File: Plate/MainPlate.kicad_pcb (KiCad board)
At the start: 2 copper layers, 139.1 x 77.2 mm, 4 parts, among them J1 Conn_01x03, SW1 Test, SW2 Service

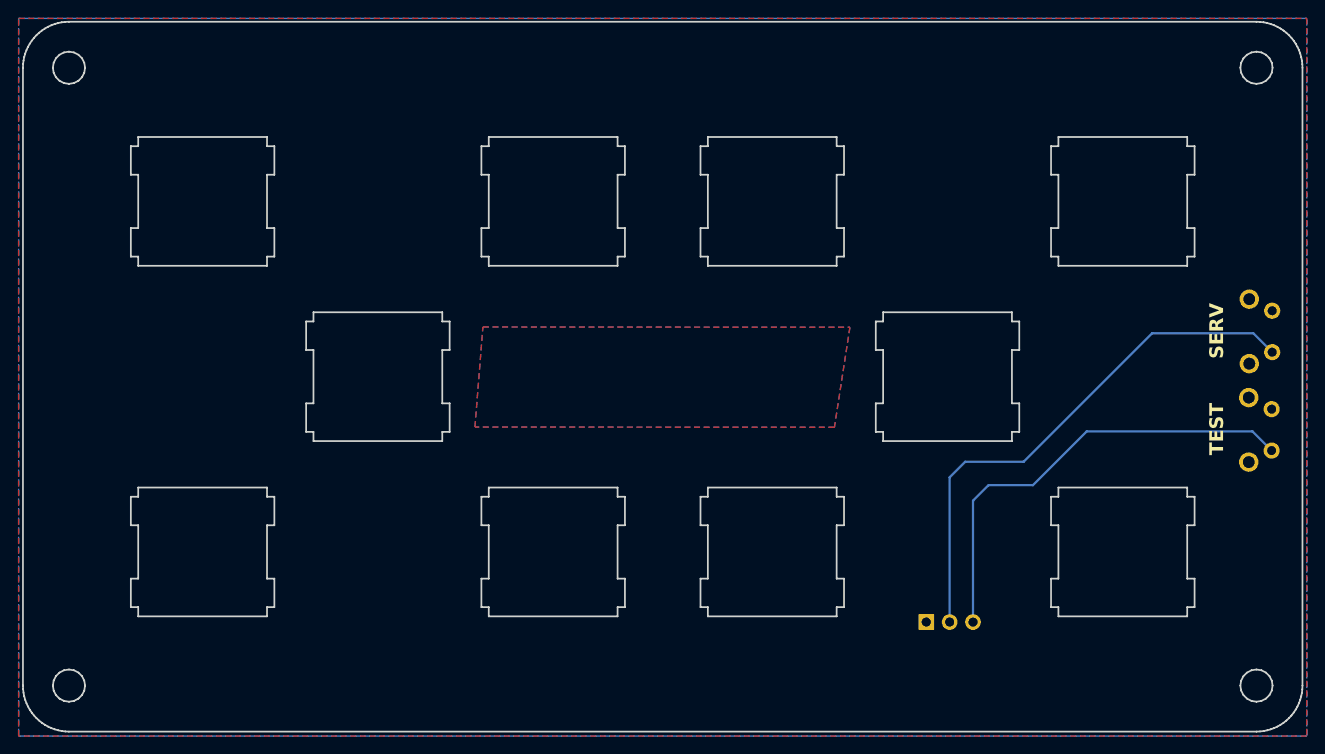
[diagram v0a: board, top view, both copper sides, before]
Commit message: fancy plate graphics, reroute all the LEDs because wrong pinout
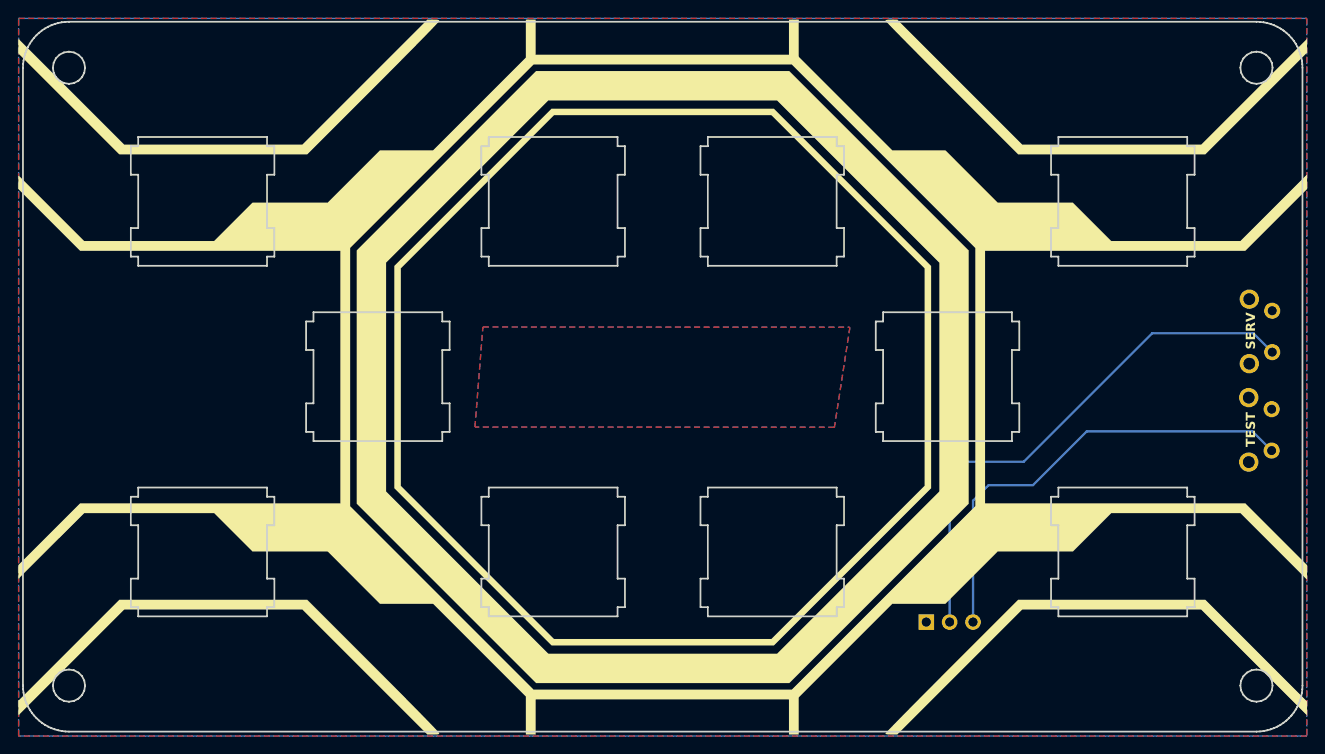
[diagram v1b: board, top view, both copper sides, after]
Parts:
- added G***: LOGO, PicoLX Graphics:Silkscreen, F.Cu at (149.8, 100.2)
- added G***: LOGO, PicoLX Graphics:Front Mask, F.Cu at (149.7, 100.2)

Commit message: Move buttons, add totally 100% real LEDs to plate
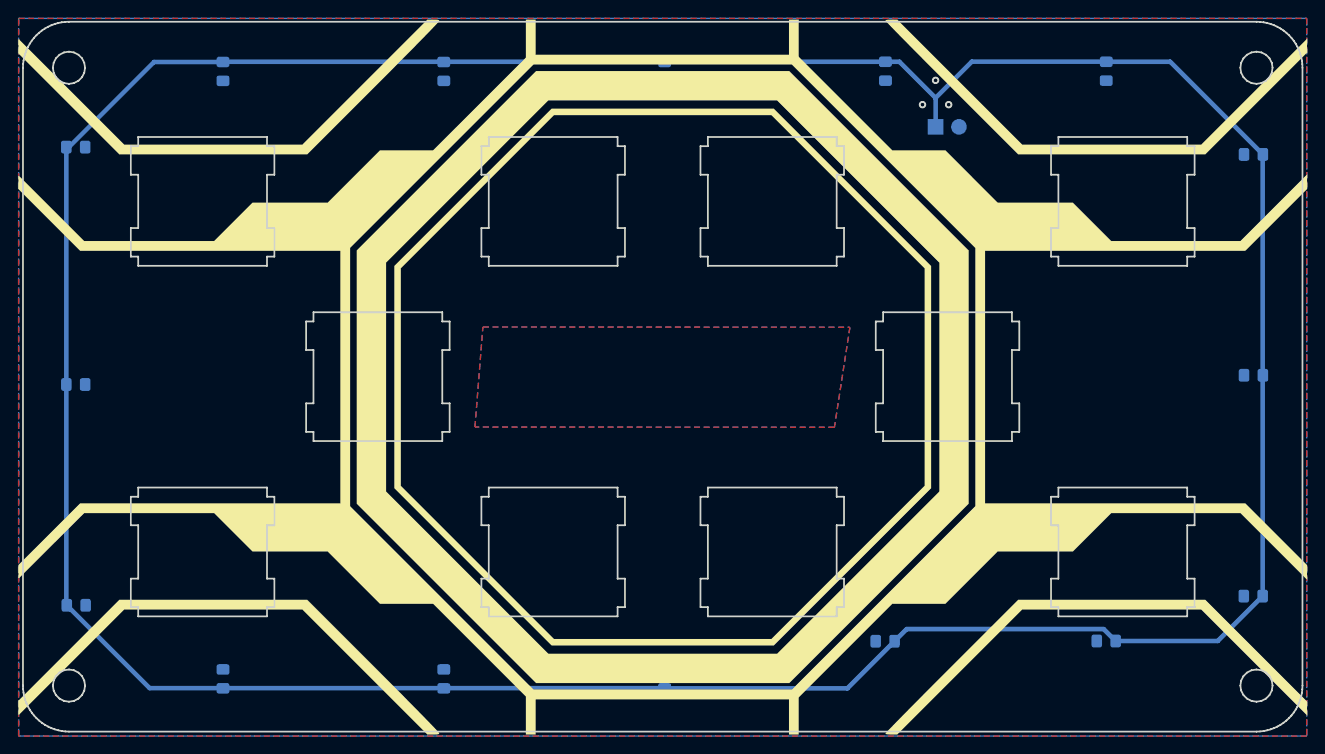
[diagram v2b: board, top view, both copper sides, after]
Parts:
- removed SW1: Test, Button_Switch_THT:SW_Tactile_SPST_Angled_PTS645Vx39-2LFS
- removed SW2: Service, Button_Switch_THT:SW_Tactile_SPST_Angled_PTS645Vx39-2LFS
- added LED1: LED_Small, LED_SMD:LED_0805_2012Metric_Pad1.15x1.40mm_HandSolder, B.Cu at (198.0, 67.0)
- added LED10: LED_Small, LED_SMD:LED_0805_2012Metric_Pad1.15x1.40mm_HandSolder, B.Cu at (126.0, 133.0)
- added LED11: LED_Small, LED_SMD:LED_0805_2012Metric_Pad1.15x1.40mm_HandSolder, B.Cu at (150.0, 133.0)
- added LED12: LED_Small, LED_SMD:LED_0805_2012Metric_Pad1.15x1.40mm_HandSolder, B.Cu at (174.0, 128.9)
- added LED13: LED_Small, LED_SMD:LED_0805_2012Metric_Pad1.15x1.40mm_HandSolder, B.Cu at (198.0, 128.9)
- added LED14: LED_Small, LED_SMD:LED_0805_2012Metric_Pad1.15x1.40mm_HandSolder, B.Cu at (214.0, 124.0)
- added LED15: LED_Small, LED_SMD:LED_0805_2012Metric_Pad1.15x1.40mm_HandSolder, B.Cu at (214.0, 100.0)
- added LED16: LED_Small, LED_SMD:LED_0805_2012Metric_Pad1.15x1.40mm_HandSolder, B.Cu at (214.0, 76.0)
- added LED2: LED_Small, LED_SMD:LED_0805_2012Metric_Pad1.15x1.40mm_HandSolder, B.Cu at (174.0, 67.0)
- added LED3: LED_Small, LED_SMD:LED_0805_2012Metric_Pad1.15x1.40mm_HandSolder, B.Cu at (150.0, 67.0)
- added LED4: LED_Small, LED_SMD:LED_0805_2012Metric_Pad1.15x1.40mm_HandSolder, B.Cu at (126.0, 67.0)
- added LED5: LED_Small, LED_SMD:LED_0805_2012Metric_Pad1.15x1.40mm_HandSolder, B.Cu at (102.0, 67.0)
- added LED6: LED_Small, LED_SMD:LED_0805_2012Metric_Pad1.15x1.40mm_HandSolder, B.Cu at (86.0, 75.2)
- added LED7: LED_Small, LED_SMD:LED_0805_2012Metric_Pad1.15x1.40mm_HandSolder, B.Cu at (86.0, 101.0)
- added LED8: LED_Small, LED_SMD:LED_0805_2012Metric_Pad1.15x1.40mm_HandSolder, B.Cu at (86.0, 125.0)
- added LED9: LED_Small, LED_SMD:LED_0805_2012Metric_Pad1.15x1.40mm_HandSolder, B.Cu at (102.0, 133.0)
- J1: value Conn_01x03 -> Conn_01x02; footprint Connector_PinHeader_2.54mm:PinHeader_1x03_P2.54mm_Vertical -> Connector_PinHeader_2.54mm:PinHeader_1x02_P2.54mm_Vertical
- moved J1 53.8 mm to (179.4, 73.0)
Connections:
- J1 pad 1: GND -> +3V3
- J1 pad 2: Net-(J1-Pin_2) -> GND
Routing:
- net +3V3: track 0.00 -> 381.2 mm
- net Net-(J1-Pin_2): track 58.1 -> 0.00 mm
- net Net-(J1-Pin_3): track 49.6 -> 0.00 mm
- net GND: vias 0 -> 3
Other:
- board text added: "+3V3"
- board text added: "GND"
- board text removed: "SERV"
- board text removed: "TEST"

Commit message: the vias looked bad from the front nvm
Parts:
- moved G*** 1.08 mm to (208.5, 134.3)
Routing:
- net GND: vias 3 -> 0
